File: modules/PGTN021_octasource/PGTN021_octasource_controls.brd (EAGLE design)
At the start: 69.8 x 100.3 mm, 87 parts

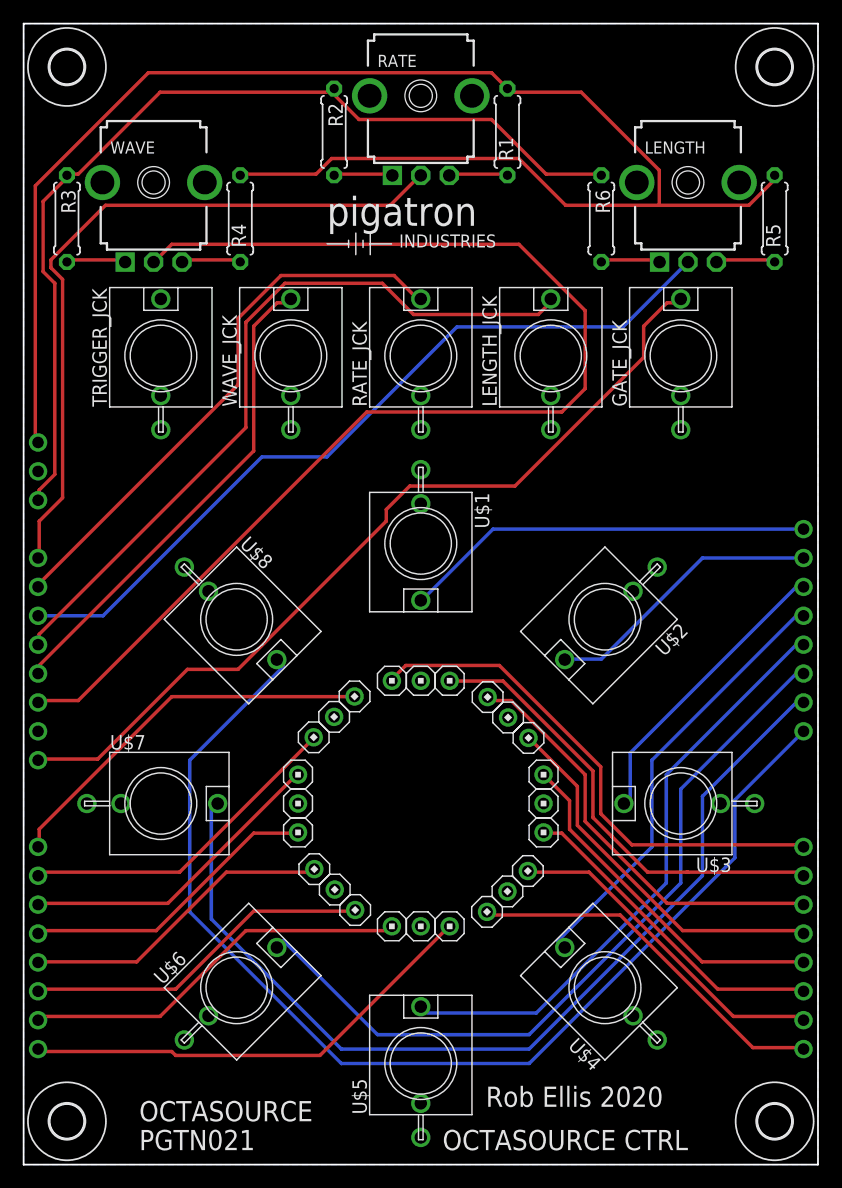
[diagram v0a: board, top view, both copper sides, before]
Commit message: Modified boards to fit together better
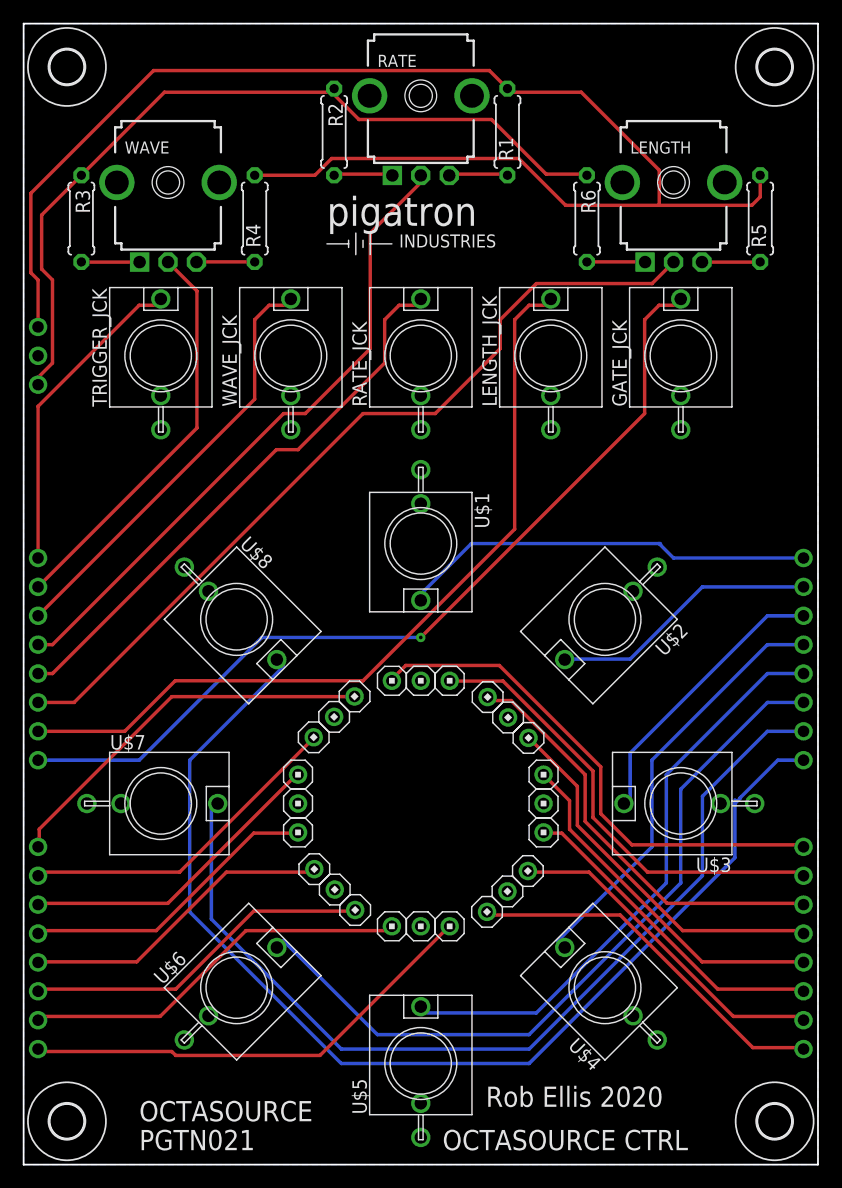
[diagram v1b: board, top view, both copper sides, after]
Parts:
- moved TRIG_IN 15.2 mm to (1.27, 53.3)
- moved GND 10.2 mm to (1.27, 71.1)
- moved +12V 10.2 mm to (1.27, 73.7)
- moved -12V 10.2 mm to (1.27, 68.6)
- moved WAVE_POT 10.2 mm to (1.27, 50.8)
- moved RATE_POT 7.62 mm to (1.27, 45.7)
- moved LENGTH_CV 7.62 mm to (1.27, 38.1)
- moved LENGTH_POT 7.62 mm to (1.27, 40.6)
- moved RATE_CV 7.62 mm to (1.27, 43.2)
- moved WAVE_CV 5.08 mm to (1.27, 48.3)
- moved OUT2 2.54 mm to (68.6, 50.8)
- moved OUT1 2.54 mm to (68.6, 53.3)
- moved OUT3 2.54 mm to (68.6, 48.3)
- moved OUT4 2.54 mm to (68.6, 45.7)
- moved OUT5 2.54 mm to (68.6, 43.2)
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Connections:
- new net N$38: TRIGGER_JCK.P$1, TRIG_IN.1
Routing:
- net N$7: track 107.4 -> 35.4 mm
- net N$38: track 0.00 -> 28.4 mm
- net -12V: track 83.9 -> 71.7 mm
- net +12V: track 139.0 -> 127.4 mm
- net N$4: track 63.1 -> 57.1 mm
- net N$11: track 66.0 -> 71.9 mm
- net N$12: track 42.8 -> 38.2 mm
- net N$10: track 70.1 -> 73.4 mm
- net N$13: track 75.6 -> 78.5 mm, vias 0 -> 1
- net N$20: track 84.2 -> 83.2 mm
- net N$17: track 38.7 -> 37.7 mm
- net N$15: track 24.7 -> 23.6 mm
- net N$16: track 26.3 -> 25.2 mm
- net N$18: track 53.2 -> 52.2 mm
- net N$19: track 68.0 -> 66.9 mm
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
